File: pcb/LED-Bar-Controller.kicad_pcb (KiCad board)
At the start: 4 copper layers, 46 x 44 mm, 43 parts, among them J1 Conn_01x03, J2 USB_C, J3 Serial, Q1 AO3400A, Q2 AO3400A, SW1 Power, SW2 Color, SW3 Bright-, SW4 Bright+, U1 ESP32-WROOM-32, U2 AMS1117-3.3

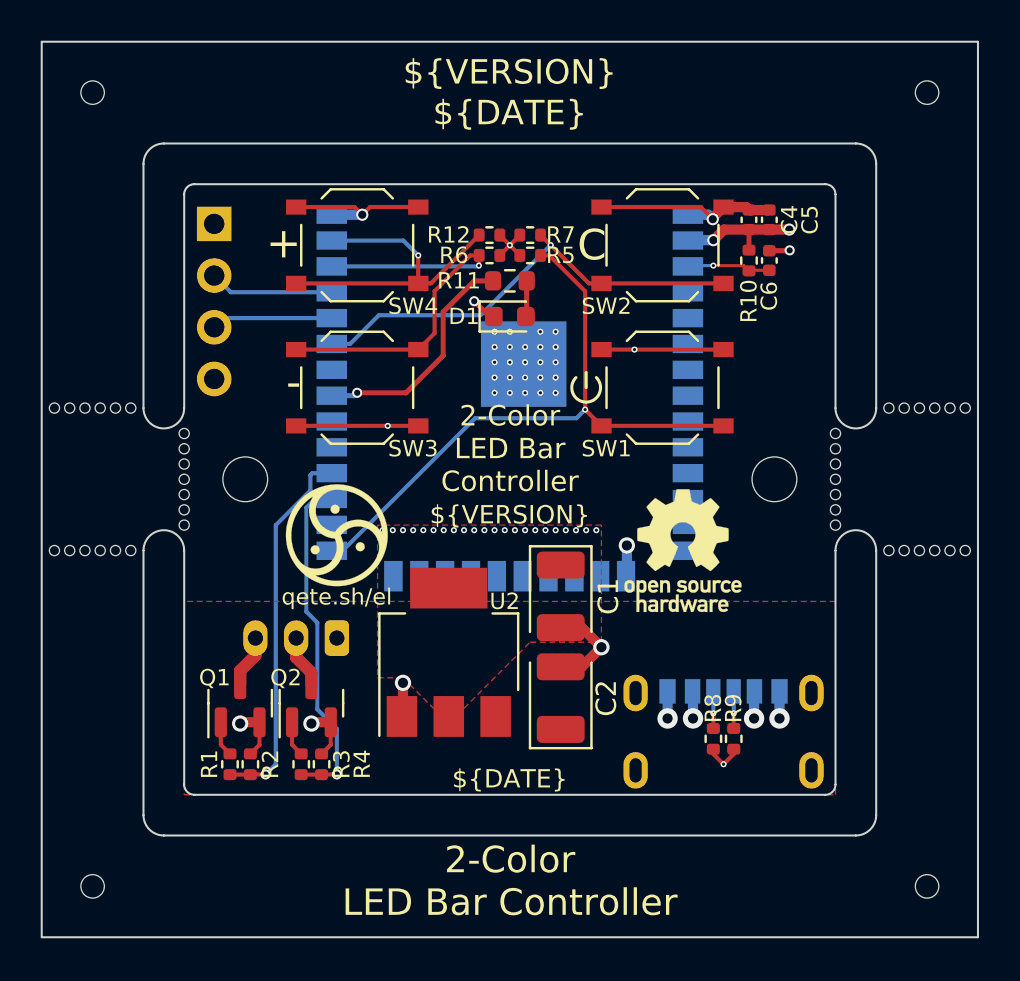
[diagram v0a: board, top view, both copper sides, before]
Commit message: style: silkscreen cleanup
Renumber parts and clean up silkscreen positioning
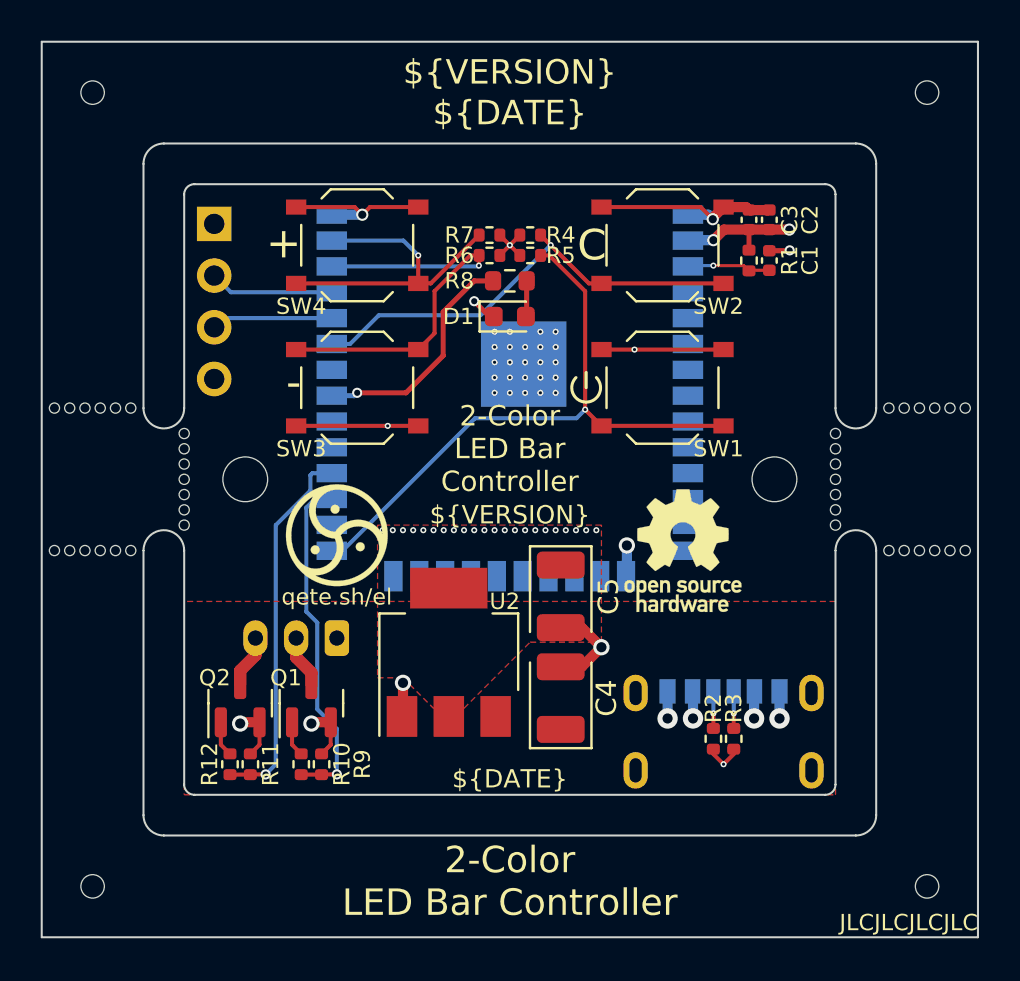
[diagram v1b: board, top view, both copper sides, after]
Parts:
- renumbered C6 to C1, C5 to C2, C4 to C3, C2 to C4, C1 to C5, J2 to J1, J3 to J2, J1 to J3, Q2 to Q1, Q1 to Q2, R10 to R1, R3 to R10, R2 to R11, R1 to R12, R8 to R2, R9 to R3, R7 to R4, R12 to R7, R11 to R8, R4 to R9
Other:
- board text added: "JLCJLCJLCJLC"
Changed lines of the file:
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@@
     (property "ki_keywords" "switch normally-open pushbutton push-button")
     (attr smd)
-    (fp_text reference "SW1" (at -2.75 3) (layer "F.SilkS")
+    (fp_text reference "SW1" (at 2.75 3) (layer "F.SilkS")
         (effects (font (size 0.8 0.8) (thickness 0.15)))
     )
@@
     (property "ki_keywords" "R resistor")
     (attr smd)
-    (fp_text reference "R6" (at 1.75 0) (layer "F.SilkS")
-        (effects (font (size 0.8 0.8) (thickness 0.15)))
+    (fp_text reference "R6" (at 0.75 0) (layer "F.SilkS")
+        (effects (font (size 0.8 0.8) (thickness 0.15)) (justify right))
     )
     (fp_text value "100k" (at 0 1.17) (layer "F.Fab")
@@
     (property "ki_keywords" "R resistor")
     (attr smd)
-    (fp_text reference "R10" (at 2 0 90) (layer "F.SilkS")
+    (fp_text reference "R1" (at 0 -2 90) (layer "F.SilkS")
         (effects (font (size 0.8 0.8) (thickness 0.15)))
     )
@@
     (property "ki_keywords" "N-Channel MOSFET")
     (attr smd)
-    (fp_text reference "Q1" (at 1.25 -1.25) (layer "F.SilkS")
+    (fp_text reference "Q2" (at 1.25 -1.25) (layer "F.SilkS")
         (effects (font (size 0.8 0.8) (thickness 0.15)))
     )
@@
     (property "ki_keywords" "N-Channel MOSFET")
     (attr smd)
-    (fp_text reference "Q2" (at 1.25 -1.25) (layer "F.SilkS")
+    (fp_text reference "Q1" (at 1.25 -1.25) (layer "F.SilkS")
         (effects (font (size 0.8 0.8) (thickness 0.15)))
     )
@@
     (property "ki_keywords" "R resistor")
     (attr smd)
-    (fp_text reference "R7" (at 1.5 -1) (layer "F.SilkS")
+    (fp_text reference "R4" (at 1.5 -1) (layer "F.SilkS")
         (effects (font (size 0.8 0.8) (thickness 0.15)))
     )
@@
     (property "ki_keywords" "R resistor")
     (attr smd)
-    (fp_text reference "R2" (at 0 1 90) (layer "F.SilkS")
+    (fp_text reference "R11" (at 0 1 90) (layer "F.SilkS")
         (effects (font (size 0.8 0.8) (thickness 0.15)))
     )
@@
     (property "ki_keywords" "switch normally-open pushbutton push-button")
     (attr smd)
-    (fp_text reference "SW2" (at -2.75 3) (layer "F.SilkS")
+    (fp_text reference "SW2" (at 2.75 3) (layer "F.SilkS")
         (effects (font (size 0.8 0.8) (thickness 0.15)))
     )
@@
     (property "ki_keywords" "capacitor cap")
     (attr smd)
-    (fp_text reference "C5" (at 0 -2 90) (layer "F.SilkS")
+    (fp_text reference "C2" (at 0 -2 90) (layer "F.SilkS")
         (effects (font (size 0.8 0.8) (thickness 0.15)))
     )
@@
     (property "ki_keywords" "R resistor")
     (attr smd)
-    (fp_text reference "R4" (at 0 2 90) (layer "F.SilkS")
+    (fp_text reference "R9" (at 0 2 90) (layer "F.SilkS")
         (effects (font (size 0.8 0.8) (thickness 0.15)))
     )
@@
     (property "ki_keywords" "switch normally-open pushbutton push-button")
     (attr smd)
-    (fp_text reference "SW4" (at 2.75 3) (layer "F.SilkS")
+    (fp_text reference "SW4" (at -2.75 3) (layer "F.SilkS")
         (effects (font (size 0.8 0.8) (thickness 0.15)))
     )
@@
     (property "ki_keywords" "R resistor")
     (attr smd)
-    (fp_text reference "R1" (at 0 -1 90) (layer "F.SilkS")
+    (fp_text reference "R12" (at 0 -1 90) (layer "F.SilkS")
         (effects (font (size 0.8 0.8) (thickness 0.15)))
     )
@@
     (property "ki_keywords" "R resistor")
     (attr smd)
-    (fp_text reference "R3" (at 0 2 90) (layer "F.SilkS")
+    (fp_text reference "R10" (at 0 2 90) (layer "F.SilkS")
         (effects (font (size 0.8 0.8) (thickness 0.15)))
     )
@@
     (property "ki_keywords" "capacitor cap")
     (attr smd)
-    (fp_text reference "C6" (at 1.75 0 90) (layer "F.SilkS")
+    (fp_text reference "C1" (at 0 -2 90) (layer "F.SilkS")
         (effects (font (size 0.8 0.8) (thickness 0.15)))
     )
@@
     (property "ki_keywords" "switch normally-open pushbutton push-button")
     (attr smd)
-    (fp_text reference "SW3" (at -2.75 -3) (layer "F.SilkS")
+    (fp_text reference "SW3" (at 2.75 -3) (layer "F.SilkS")
         (effects (font (size 0.8 0.8) (thickness 0.15)))
     )
@@
     (property "ki_keywords" "cap capacitor")
     (attr smd)
-    (fp_text reference "C1" (at 0 -2.35 90) (layer "F.SilkS")
+    (fp_text reference "C5" (at 0 -2.35 90) (layer "F.SilkS")
         (effects (font (size 1 1) (thickness 0.15)))
     )
@@
     (property "ki_keywords" "R resistor")
     (attr smd)
-    (fp_text reference "R8" (at -1.5 0 90) (layer "F.SilkS")
+    (fp_text reference "R2" (at -1.5 0 90) (layer "F.SilkS")
         (effects (font (size 0.8 0.8) (thickness 0.15)))
     )
@@
     (property "ki_keywords" "LED diode")
     (attr smd)
-    (fp_text reference "D1" (at -2.25 0) (layer "F.SilkS")
-        (effects (font (size 0.8 0.8) (thickness 0.15)))
+    (fp_text reference "D1" (at -1.75 0) (layer "F.SilkS")
+        (effects (font (size 0.8 0.8) (thickness 0.15)) (justify right))
     )
     (fp_text value "LED" (at 0 1.43) (layer "F.Fab")
@@
     (property "ki_keywords" "capacitor cap")
     (attr smd)
-    (fp_text reference "C4" (at 0 -2 -90) (layer "F.SilkS")
+    (fp_text reference "C3" (at 0 -2 -90) (layer "F.SilkS")
         (effects (font (size 0.8 0.8) (thickness 0.15)))
     )
@@
     (property "ki_keywords" "cap capacitor")
     (attr smd)
-    (fp_text reference "C2" (at 0 2.25 270) (layer "F.SilkS")
+    (fp_text reference "C4" (at 0 2.25 270) (layer "F.SilkS")
         (effects (font (size 1 1) (thickness 0.15)))
     )
@@
     (property "ki_keywords" "R resistor")
     (attr smd)
-    (fp_text reference "R11" (at -2.5 0) (layer "F.SilkS")
-        (effects (font (size 0.8 0.8) (thickness 0.15)))
+    (fp_text reference "R8" (at -1.75 0) (layer "F.SilkS")
+        (effects (font (size 0.8 0.8) (thickness 0.15)) (justify right))
     )
     (fp_text value "680R" (at 0 1.43) (layer "F.Fab")
@@
     (property "ki_keywords" "R resistor")
     (attr smd)
-    (fp_text reference "R9" (at -1.5 0 90) (layer "F.SilkS")
+    (fp_text reference "R3" (at -1.5 0 90) (layer "F.SilkS")
         (effects (font (size 0.8 0.8) (thickness 0.15)))
     )
@@
     (property "ki_keywords" "R resistor")
     (attr smd)
-    (fp_text reference "R12" (at 2 0) (layer "F.SilkS")
-        (effects (font (size 0.8 0.8) (thickness 0.15)))
+    (fp_text reference "R7" (at 0.75 0) (layer "F.SilkS")
+        (effects (font (size 0.8 0.8) (thickness 0.15)) (justify right))
     )
     (fp_text value "100k" (at 0 1.17) (layer "F.Fab")
@@
     (property "ki_keywords" "usb universal serial bus type-C power-only charging-only 6P 6C")
     (attr through_hole)
-    (fp_text reference "J2" (at 0 1.5) (layer "B.SilkS")
+    (fp_text reference "J1" (at 0 1.5) (layer "B.SilkS")
         (effects (font (size 0.8 0.8) (thickness 0.15)) (justify mirror))
     )
@@
     (property "ki_keywords" "connector")
     (attr through_hole)
-    (fp_text reference "J1" (at 2 -2.95) (layer "B.SilkS")
+    (fp_text reference "J3" (at 2 -2.95) (layer "B.SilkS")
         (effects (font (size 0.8 0.8) (thickness 0.15)) (justify mirror))
     )
@@
     (property "ki_keywords" "connector")
     (attr through_hole)
-    (fp_text reference "J3" (at 0 2.77 90) (layer "B.SilkS") hide
+    (fp_text reference "J2" (at 0 2.77 90) (layer "B.SilkS") hide
         (effects (font (size 0.8 0.8) (thickness 0.15)) (justify mirror))
     )
@@
     (effects (font (size 1.2 1.2) (thickness 0.15)))
   )
+  (gr_text "JLCJLCJLCJLC" (at 161.75 122.25) (layer "F.SilkS")
+    (effects (font (size 0.8 0.8) (thickness 0.15)) (justify right bottom))
+  )
   (gr_text "2-Color\nLED Bar Controller" (at 138.75 119.75) (layer "F.SilkS")

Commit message: fix: replace too small vias
Used too small vias for normal production with JLCPCB
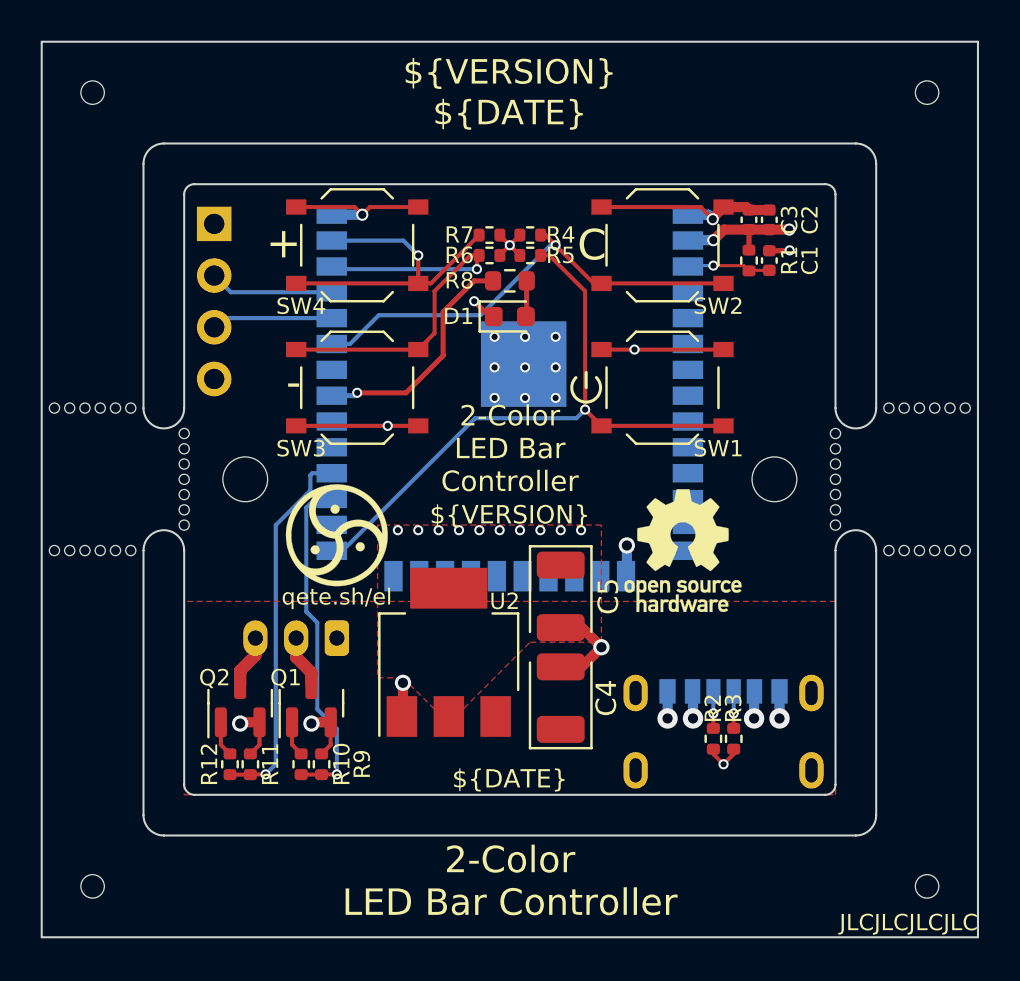
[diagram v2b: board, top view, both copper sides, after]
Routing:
- net GND: vias 38 -> 23
- net +3V3: vias 25 -> 13
